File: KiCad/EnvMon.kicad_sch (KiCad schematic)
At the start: 29 parts, among them J1 USB-C, J2 DC, J3 GPIO, M1 SCD30-4pin, M2 OLED1.5-RGB, U1 LMR16006YQ3, U2 FT231XQ, U3 ESP32-WROOM-32

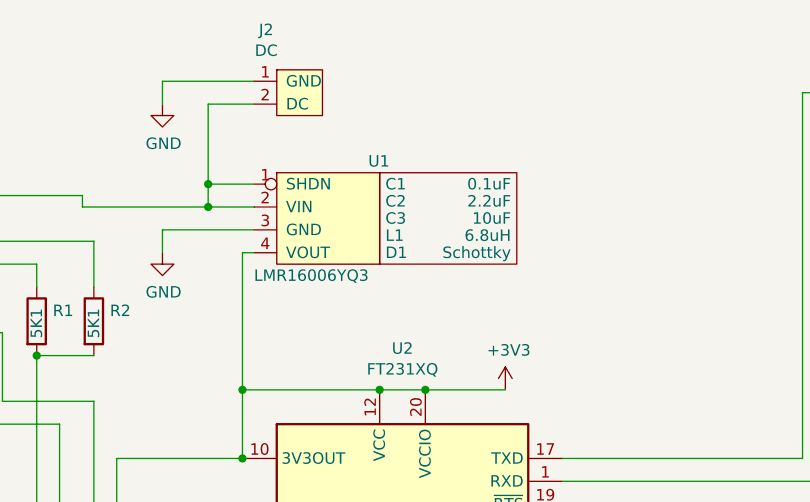
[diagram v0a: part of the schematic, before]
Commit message: More KiCad 6 tweaks
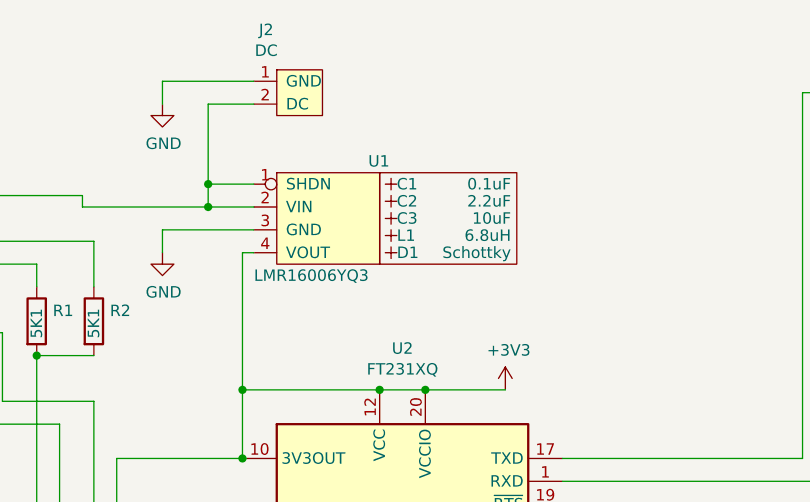
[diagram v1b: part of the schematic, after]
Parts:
- U3: footprint RevK:ESP32-WROOM-32 -> RF_Module:ESP32-WROOM-32
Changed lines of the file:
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@@
   (title_block
     (title "1.5\" OLED Module driver with GPIO")
-    (date "2021-07-20")
+    (date "${DATE}")
     (rev "4")
     (company "Adrian Kennard / Andrews & Arnold Ltd")
@@
     (property "Reference" "U3" (id 0) (at 203.2 106.045 0))
     (property "Value" "ESP32-WROOM-32" (id 1) (at 224.155 105.41 0))
-    (property "Footprint" "RevK:ESP32-WROOM-32" (id 2) (at 213.995 108.585 0)
+    (property "Footprint" "RF_Module:ESP32-WROOM-32" (id 2) (at 213.995 108.585 0)
       (effects (font (size 1.27 1.27)) hide)
     )
@@
   (symbol (lib_id "RevK:Hidden") (at 100.965 26.035 0) (unit 1)
     (in_bom yes) (on_board yes)
-    (property "Reference" "C1" (id 0) (at 100.33 26.035 0)
+    (property "Reference" "C1" (id 0) (at 101.6 26.035 0)
       (effects (font (size 1.27 1.27)) (justify left))
     )
@@
       (effects (font (size 1.27 1.27)) hide)
     )
+    (property "Part No" "" (id 5) (at 100.965 26.035 0)
+      (effects (font (size 1.27 1.27)) hide)
+    )
     (pin "~")
   )
   (symbol (lib_id "RevK:Hidden") (at 100.965 27.94 0) (unit 1)
     (in_bom yes) (on_board yes)
-    (property "Reference" "C2" (id 0) (at 100.33 27.94 0)
+    (property "Reference" "C2" (id 0) (at 101.6 27.94 0)
       (effects (font (size 1.27 1.27)) (justify left))
     )
@@
       (effects (font (size 1.27 1.27)) hide)
     )
+    (property "Part No" "" (id 5) (at 100.965 27.94 0)
+      (effects (font (size 1.27 1.27)) hide)
+    )
     (pin "~")
   )
   (symbol (lib_id "RevK:Hidden") (at 100.965 29.845 0) (unit 1)
     (in_bom yes) (on_board yes)
-    (property "Reference" "C3" (id 0) (at 100.33 29.845 0)
+    (property "Reference" "C3" (id 0) (at 101.6 29.845 0)
       (effects (font (size 1.27 1.27)) (justify left))
     )
@@
       (effects (font (size 1.27 1.27)) hide)
     )
+    (property "Part No" "" (id 5) (at 100.965 29.845 0)
+      (effects (font (size 1.27 1.27)) hide)
+    )
     (pin "~")
   )
   (symbol (lib_id "RevK:Hidden") (at 100.965 31.75 0) (unit 1)
     (in_bom yes) (on_board yes)
-    (property "Reference" "L1" (id 0) (at 100.33 31.75 0)
+    (property "Reference" "L1" (id 0) (at 101.6 31.75 0)
       (effects (font (size 1.27 1.27)) (justify left))
     )
@@
       (effects (font (size 1.27 1.27)) hide)
     )
+    (property "Note" "" (id 6) (at 100.965 31.75 0)
+      (effects (font (size 1.27 1.27)) hide)
+    )
     (pin "~")
   )
   (symbol (lib_id "RevK:Hidden") (at 100.965 33.655 0) (unit 1)
     (in_bom yes) (on_board yes)
-    (property "Reference" "D1" (id 0) (at 100.33 33.655 0)
+    (property "Reference" "D1" (id 0) (at 101.6 33.655 0)
       (effects (font (size 1.27 1.27)) (justify left))
     )
@@
     )
     (property "Part No" "CD1206-B2100" (id 5) (at 100.965 33.655 0)
+      (effects (font (size 1.27 1.27)) hide)
+    )
+    (property "Note" "" (id 6) (at 100.965 33.655 0)
       (effects (font (size 1.27 1.27)) hide)
     )
@@
     )
     (path "/00000000-0000-0000-0000-000060467763"
-      (reference "U3") (unit 1) (value "ESP32-WROOM-32") (footprint "RevK:ESP32-WROOM-32")
-    )
-  )
+      (reference "U3") (unit 1) (value "ESP32-WROOM-32") (footprint "RF_Module:ESP32-WROOM-32")
+    )
+  )

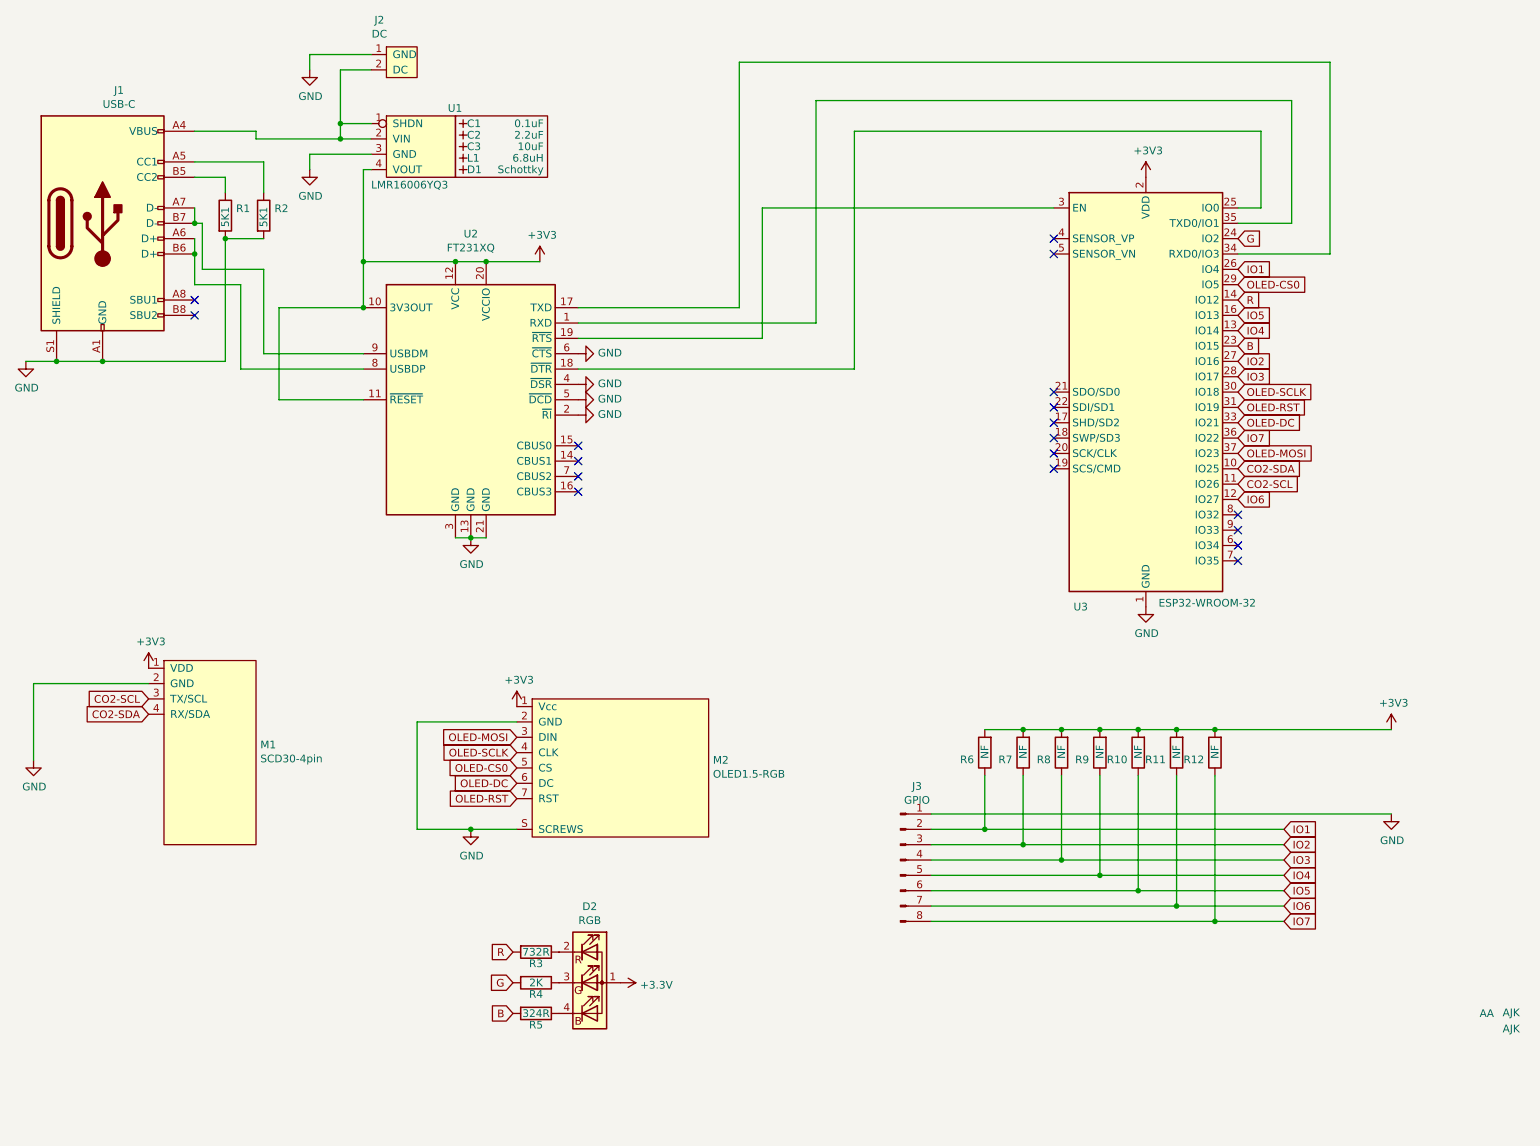
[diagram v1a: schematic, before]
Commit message: New PSU
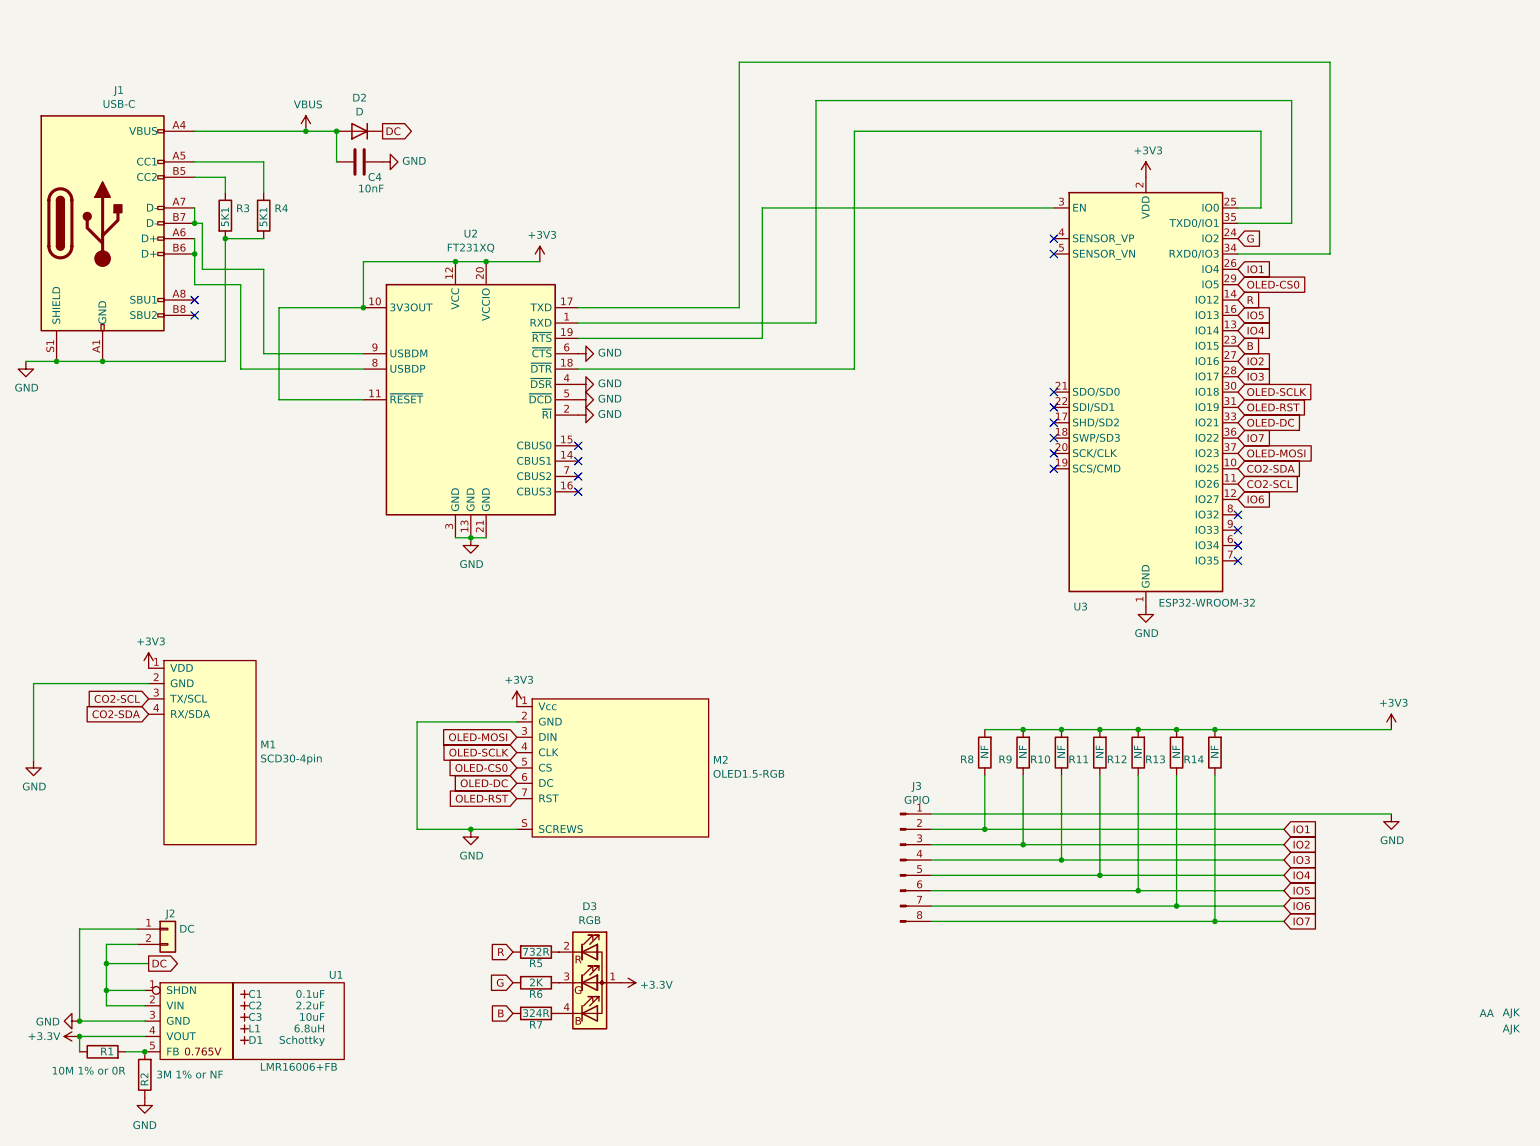
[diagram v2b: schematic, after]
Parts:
- removed J2: DC, RevK:DC, symbol RevK:DC
- removed U1: LMR16006YQ3, RevK:RegulatorBlock, symbol RevK:LMR16006YQ3
- added C4: 10nF, RevK:C_0603, symbol Device:C
- added D2: D, Diode_SMD:D_1206_3216Metric, symbol Device:D
- added J2: DC, Connector_PinHeader_2.54mm:PinHeader_1x02_P2.54mm_Vertical, symbol RevK:PowerIn
- added R1: 10M 1% or 0R, RevK:R_0603, symbol Device:R
- added R2: 3M 1% or NF, RevK:R_0603, symbol Device:R
- added U1: LMR16006+FB, RevK:RegulatorBlockFB, symbol RevK:LMR16006+FB
- U3: footprint RF_Module:ESP32-WROOM-32 -> RevK:ESP32-WROOM-32
- renumbered D2 to D3, R8 to R10, R9 to R11, R10 to R12, R11 to R13, R12 to R14, R1 to R3, R2 to R4, R3 to R5, R4 to R6, R5 to R7, R6 to R8, R7 to R9
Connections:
- net +3V3: now also R1.1, U1.4 (VOUT)
- net GND: now also C4.1, J2.1 (Pin_1), R2.1, U1.3 (GND)
- net VBUS: now reaches J1.A4 (VBUS), J1.A9 (VBUS), J1.B4 (VBUS), J1.B9 (VBUS)
- net VBUS: now also C4.2, D2.2 (A)
- new net: R1.2, R2.2, U1.5 (FB)
- new net DC: D2.1 (K), J2.2 (Pin_2), U1.1 (SHDN), U1.2 (VIN)
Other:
- moved on the sheet: C1, C2, C3, D1, L1

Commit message: Notes
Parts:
- removed U3: ESP32-WROOM-32, RevK:ESP32-WROOM-32, symbol RF_Module:ESP32-WROOM-32
- added U3: ESP32-WROOM-32, RevK:ESP32-WROOM-32, symbol RevK:ESP32-WROOM-32
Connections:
- net +3V3: now also U3.2 (VDD)
- net B: now also U3.23 (IO15)
- net CO2-SCL: now also U3.11 (IO26)
- net CO2-SDA: now also U3.10 (IO25)
- net G: now also U3.24 (IO2)
- net GND: now also U3.1 (GND), U3.15 (GND), U3.38 (GND), U3.39 (GND)
- net IO1: now also U3.26 (IO4)
- net IO2: now also U3.27 (IO16)
- net IO3: now also U3.28 (IO17)
- net IO4: now also U3.13 (IO14)
- net IO5: now also U3.16 (IO13)
- net IO6: now also U3.12 (IO27)
- net IO7: now also U3.36 (IO22)
- net OLED-CS0: now also U3.29 (IO5)
- net OLED-DC: now also U3.33 (IO21)
- net OLED-MOSI: now also U3.37 (IO23)
- net OLED-RST: now also U3.31 (IO19)
- net OLED-SCLK: now also U3.30 (IO18)
- net R: now also U3.14 (IO12)
- net at U2.18 (~{DTR}): now also U3.25 (IO0)
- net at U2.19 (~{RTS}): now also U3.3 (EN)
- net at U2.17 (TXD): now also U3.34 (RXD0/IO3)
- net at U2.1 (RXD): now also U3.35 (TXD0/IO1)
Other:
- note added: "TODO Update for VBUS. Dangerous GPIO pins. Make SCD41 version. ESP32 MINI PICO version."

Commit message: Resitors
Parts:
- R1: value 10M 1% or 0R -> 100k 1% or 0R
- R2: value 3M 1% or NF -> 30k 1% or NF
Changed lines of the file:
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@@
       (effects (font (size 1.27 1.27)) (justify left))
     )
-    (property "Value" "10M 1% or 0R" (id 1) (at 45.085 182.88 90)
+    (property "Value" "100k 1% or 0R" (id 1) (at 45.085 182.88 90)
       (effects (font (size 1.27 1.27)) (justify left))
     )
@@
       (effects (font (size 1.27 1.27)) (justify right))
     )
-    (property "Value" "3M 1% or NF" (id 1) (at 50.165 183.515 0)
+    (property "Value" "30k 1% or NF" (id 1) (at 50.165 183.515 0)
       (effects (font (size 1.27 1.27)) (justify right))
     )
@@
     )
     (path "/6324f539-5157-429d-ad08-999e5f3ad633"
-      (reference "R1") (unit 1) (value "10M 1% or 0R") (footprint "RevK:R_0603")
+      (reference "R1") (unit 1) (value "100k 1% or 0R") (footprint "RevK:R_0603")
     )
     (path "/e632df6d-ccd6-4691-adc1-89013dd5fd28"
-      (reference "R2") (unit 1) (value "3M 1% or NF") (footprint "RevK:R_0603")
+      (reference "R2") (unit 1) (value "30k 1% or NF") (footprint "RevK:R_0603")
     )
     (path "/00000000-0000-0000-0000-0000604938d6"

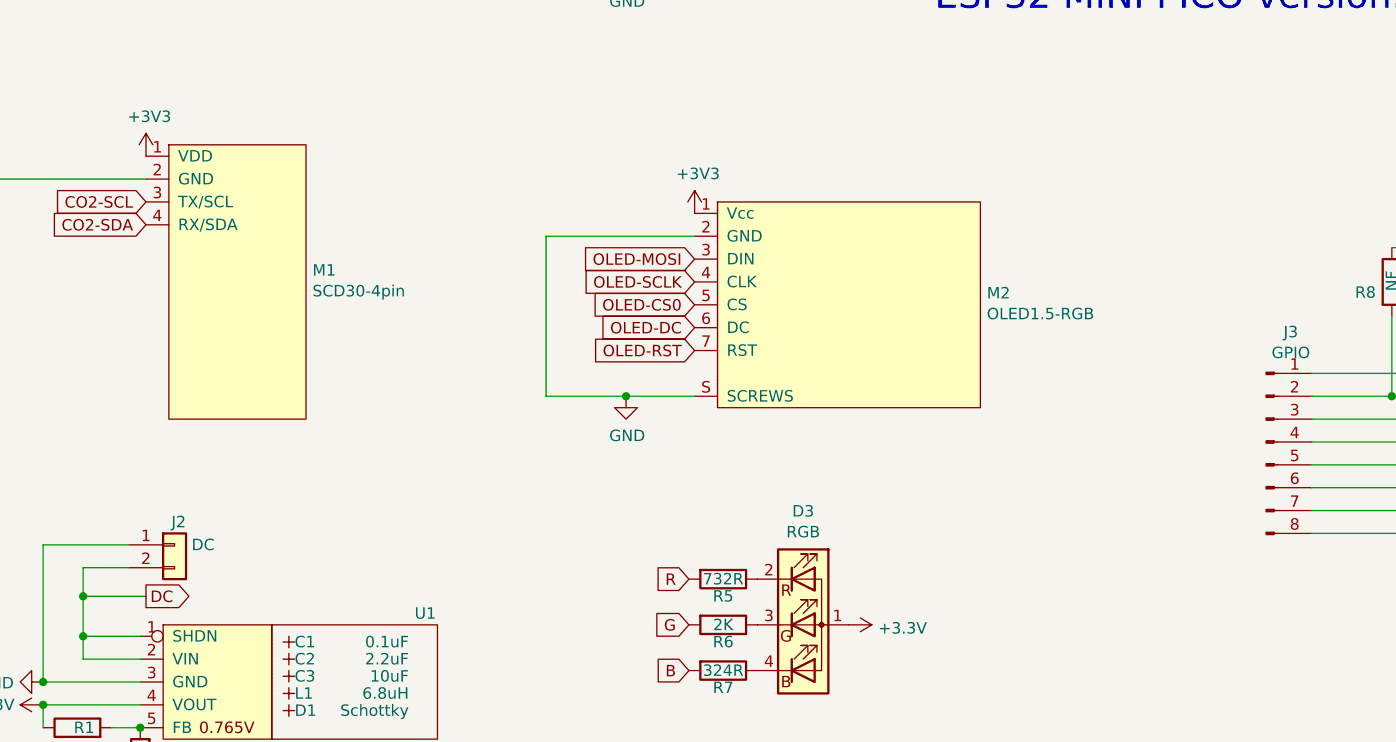
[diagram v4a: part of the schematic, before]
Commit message: Smaller holes
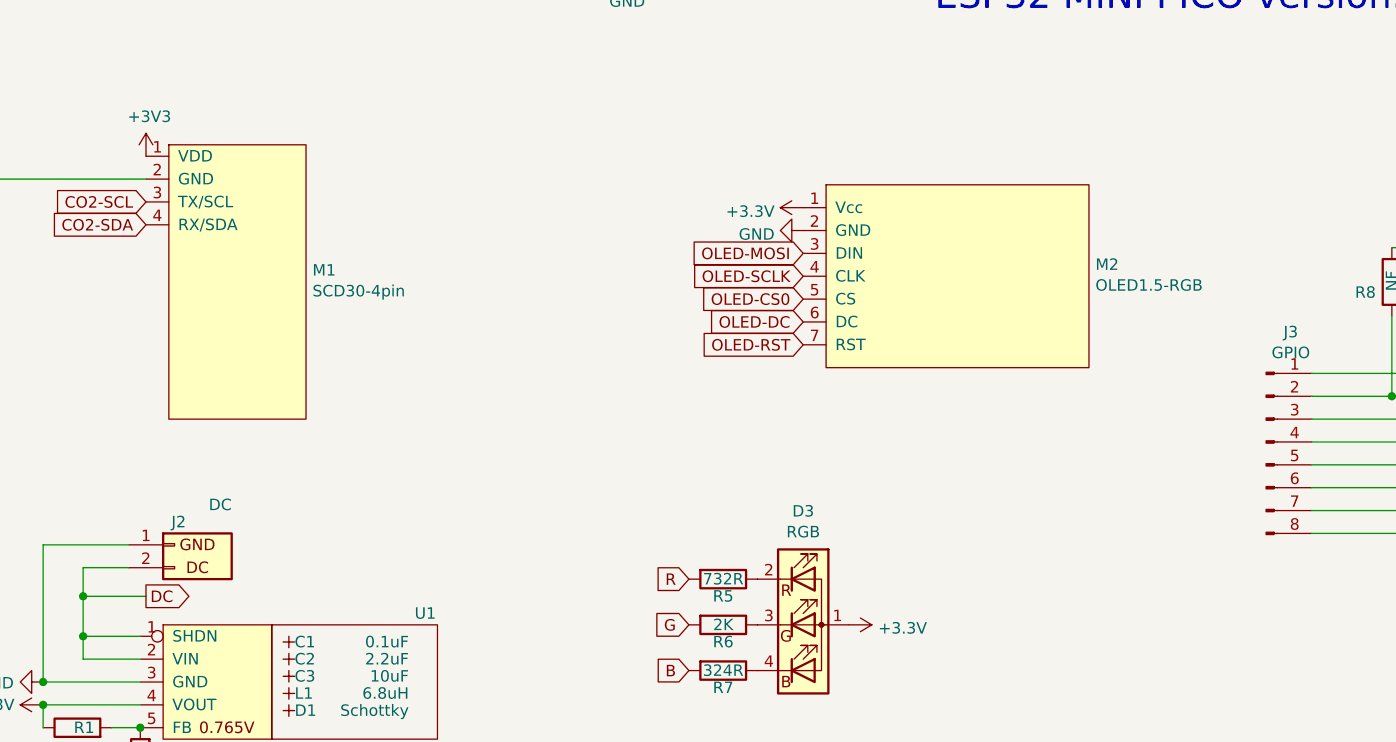
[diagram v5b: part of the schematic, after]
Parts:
- D2: footprint Diode_SMD:D_1206_3216Metric -> RevK:D_1206
- J2: footprint Connector_PinHeader_2.54mm:PinHeader_1x02_P2.54mm_Vertical -> RevK:DC; now left out of the parts list
- Logo1, Logo2, Logo3: Note (none) -> Non part, PCB printed; now left out of the parts list
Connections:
- net GND: no longer M2.S (SCREWS)
